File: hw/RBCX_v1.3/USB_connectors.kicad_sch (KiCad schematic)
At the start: 24 parts, among them J49 Conn_01x04, J50 Conn_01x04, U21 USB_C, U22 AP33772

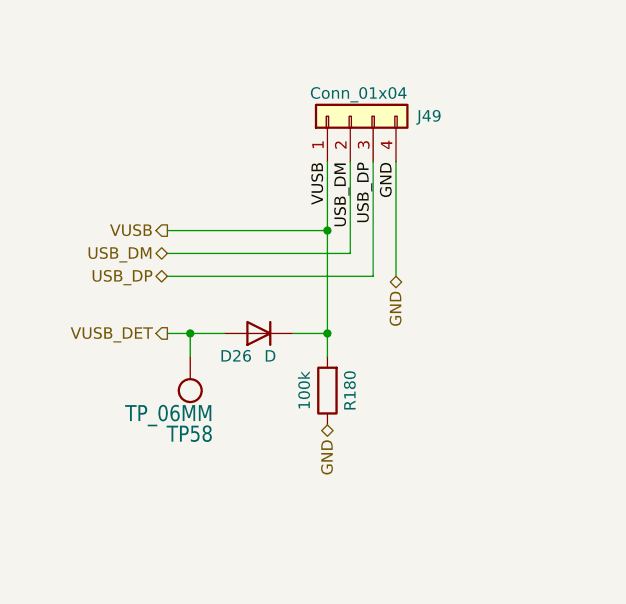
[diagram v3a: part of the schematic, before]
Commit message: USB-DET level shifter
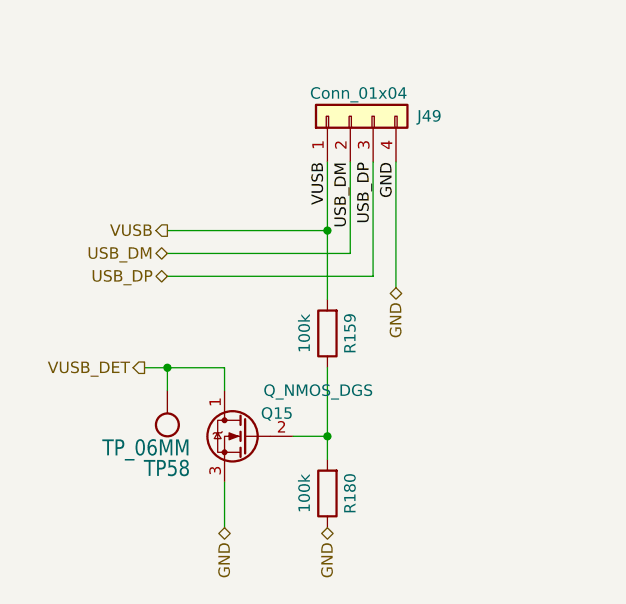
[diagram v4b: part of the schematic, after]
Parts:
- removed D26: D, Diode_SMD:D_SOD-523, symbol Device:D
- added Q15: Q_NMOS_DGS, Package_TO_SOT_SMD:SOT-723, symbol Device:Q_NMOS_DGS
- added R159: 100k, Capacitor_SMD:C_0201_0603Metric, symbol Device:R
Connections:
- net GND: now also Q15.3 (S)
- net VUSB: now also R159.2; no longer R180.2
- net VUSB_DET: now also Q15.1 (D)
- new net: Q15.2 (G), R159.1, R180.2
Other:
- moved on the sheet: R180, TP58
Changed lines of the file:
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@@
   (junction (at 220.98 54.61) (diameter 0) (color 0 0 0 0)
   )
-  (junction (at 86.36 140.97) (diameter 0) (color 0 0 0 0)
+  (junction (at 83.82 144.78) (diameter 0) (color 0 0 0 0)
   )
   (junction (at 153.67 44.45) (diameter 0) (color 0 0 0 0)
@@
   (junction (at 173.99 62.23) (diameter 0) (color 0 0 0 0)
   )
-  (junction (at 101.6 140.97) (diameter 0) (color 0 0 0 0)
+  (junction (at 101.6 152.4) (diameter 0) (color 0 0 0 0)
   )
   (junction (at 82.55 64.77) (diameter 0) (color 0 0 0 0)
@@
     (stroke (width 0) (type default) (color 0 0 0 0))
   )
-  (wire (pts (xy 86.36 140.97) (xy 90.17 140.97))
-    (stroke (width 0) (type default) (color 0 0 0 0))
-  )
   (wire (pts (xy 153.67 44.45) (xy 163.83 44.45))
     (stroke (width 0) (type default) (color 0 0 0 0))
@@
     (stroke (width 0) (type default) (color 0 0 0 0))
   )
+  (wire (pts (xy 83.82 144.78) (xy 90.17 144.78))
+    (stroke (width 0) (type default) (color 0 0 0 0))
+  )
   (wire (pts (xy 132.08 78.74) (xy 132.08 76.2))
     (stroke (width 0) (type default) (color 0 0 0 0))
@@
     (stroke (width 0) (type default) (color 0 0 0 0))
   )
-  (wire (pts (xy 101.6 140.97) (xy 101.6 143.51))
+  (wire (pts (xy 101.6 152.4) (xy 101.6 154.94))
     (stroke (width 0) (type default) (color 0 0 0 0))
   )
@@
     (stroke (width 0) (type default) (color 0 0 0 0))
   )
+  (wire (pts (xy 101.6 144.78) (xy 101.6 152.4))
+    (stroke (width 0) (type default) (color 0 0 0 0))
+  )
   (wire (pts (xy 189.23 67.31) (xy 173.99 67.31))
     (stroke (width 0) (type default) (color 0 0 0 0))
@@
     (stroke (width 0) (type default) (color 0 0 0 0))
   )
-  (wire (pts (xy 109.22 121.92) (xy 109.22 134.62))
+  (wire (pts (xy 109.22 121.92) (xy 109.22 135.89))
     (stroke (width 0) (type default) (color 0 0 0 0))
   )
@@
     (stroke (width 0) (type default) (color 0 0 0 0))
   )
-  (wire (pts (xy 83.82 140.97) (xy 86.36 140.97))
+  (wire (pts (xy 90.17 144.78) (xy 90.17 147.32))
+    (stroke (width 0) (type default) (color 0 0 0 0))
+  )
+  (wire (pts (xy 81.28 144.78) (xy 83.82 144.78))
     (stroke (width 0) (type default) (color 0 0 0 0))
   )
@@
     (stroke (width 0) (type default) (color 0 0 0 0))
   )
-  (wire (pts (xy 97.79 140.97) (xy 101.6 140.97))
+  (wire (pts (xy 97.79 152.4) (xy 101.6 152.4))
     (stroke (width 0) (type default) (color 0 0 0 0))
   )
@@
     (stroke (width 0) (type default) (color 0 0 0 0))
   )
-  (wire (pts (xy 101.6 140.97) (xy 101.6 129.54))
+  (wire (pts (xy 101.6 129.54) (xy 101.6 137.16))
     (stroke (width 0) (type default) (color 0 0 0 0))
   )
@@
     (stroke (width 0) (type default) (color 0 0 0 0))
   )
-  (wire (pts (xy 86.36 143.51) (xy 86.36 140.97))
+  (wire (pts (xy 83.82 147.32) (xy 83.82 144.78))
     (stroke (width 0) (type default) (color 0 0 0 0))
   )
@@
   )
   (wire (pts (xy 76.2 54.61) (xy 76.2 76.2))
+    (stroke (width 0) (type default) (color 0 0 0 0))
+  )
+  (wire (pts (xy 90.17 162.56) (xy 90.17 157.48))
     (stroke (width 0) (type default) (color 0 0 0 0))
   )
@@
     (effects (font (size 1.27 1.27)) (justify right))
   )
+  (hierarchical_label "GND" (shape bidirectional) (at 90.17 162.56 270)
+    (effects (font (size 1.27 1.27)) (justify right))
+  )
   (hierarchical_label "GND" (shape input) (at 248.92 102.87 270)
     (effects (font (size 1.27 1.27)) (justify right))
@@
     (effects (font (size 1.27 1.27)) (justify right))
   )
-  (hierarchical_label "VUSB_DET" (shape output) (at 83.82 140.97 180)
+  (hierarchical_label "VUSB_DET" (shape output) (at 81.28 144.78 180)
     (effects (font (size 1.27 1.27)) (justify right))
   )
@@
     (effects (font (size 1.27 1.27)) (justify right))
   )
-  (hierarchical_label "GND" (shape bidirectional) (at 109.22 134.62 270)
+  (hierarchical_label "GND" (shape bidirectional) (at 109.22 135.89 270)
     (effects (font (size 1.27 1.27)) (justify right))
   )
@@
     (effects (font (size 1.27 1.27)) (justify right))
   )
-  (hierarchical_label "GND" (shape bidirectional) (at 101.6 151.13 270)
+  (hierarchical_label "GND" (shape bidirectional) (at 101.6 162.56 270)
     (effects (font (size 1.27 1.27)) (justify right))
   )
@@
     (pin "2")
   )
-  (symbol (lib_id "Device:R") (at 101.6 147.32 180) (unit 1)
-    (in_bom yes) (on_board yes)
-    (property "Reference" "R180" (id 0) (at 104.14 147.32 90))
-    (property "Value" "100k" (id 1) (at 99.06 147.32 90))
-    (property "Footprint" "Capacitor_SMD:C_0201_0603Metric" (id 2) (at 103.378 147.32 90)
-      (effects (font (size 1.27 1.27)) hide)
-    )
-    (property "Datasheet" "~" (id 3) (at 101.6 147.32 0)
-      (effects (font (size 1.27 1.27)) hide)
-    )
-    (property "LCSC" "C270364" (id 4) (at 101.6 147.32 0)
-      (effects (font (size 1.27 1.27)) hide)
-    )
-    (property "Basic/Extended" "E" (id 5) (at 101.6 147.32 0)
+  (symbol (lib_id "Device:R") (at 101.6 158.75 180) (unit 1)
+    (in_bom yes) (on_board yes)
+    (property "Reference" "R180" (id 0) (at 104.14 158.75 90))
+    (property "Value" "100k" (id 1) (at 99.06 158.75 90))
+    (property "Footprint" "Capacitor_SMD:C_0201_0603Metric" (id 2) (at 103.378 158.75 90)
+      (effects (font (size 1.27 1.27)) hide)
+    )
+    (property "Datasheet" "~" (id 3) (at 101.6 158.75 0)
+      (effects (font (size 1.27 1.27)) hide)
+    )
+    (property "LCSC" "C270364" (id 4) (at 101.6 158.75 0)
+      (effects (font (size 1.27 1.27)) hide)
+    )
+    (property "Basic/Extended" "E" (id 5) (at 101.6 158.75 0)
       (effects (font (size 1.27 1.27)) hide)
     )
@@
     (pin "3")
     (pin "4")
+  )
+  (symbol (lib_id "Device:R") (at 101.6 140.97 180) (unit 1)
+    (in_bom yes) (on_board yes)
+    (property "Reference" "R159" (id 0) (at 104.14 140.97 90))
+    (property "Value" "100k" (id 1) (at 99.06 140.97 90))
+    (property "Footprint" "Capacitor_SMD:C_0201_0603Metric" (id 2) (at 103.378 140.97 90)
+      (effects (font (size 1.27 1.27)) hide)
+    )
+    (property "Datasheet" "~" (id 3) (at 101.6 140.97 0)
+      (effects (font (size 1.27 1.27)) hide)
+    )
+    (property "LCSC" "C270364" (id 4) (at 101.6 140.97 0)
+      (effects (font (size 1.27 1.27)) hide)
+    )
+    (property "Basic/Extended" "E" (id 5) (at 101.6 140.97 0)
+      (effects (font (size 1.27 1.27)) hide)
+    )
+    (pin "1")
+    (pin "2")
   )
   (symbol (lib_id "Device:R") (at 248.92 99.06 180) (unit 1)
@@
     (pin "4")
   )
-  (symbol (lib_id "RBCX-eagle-import:TP_06MM") (at 86.36 143.51 180) (unit 1)
-    (in_bom yes) (on_board yes)
-    (property "Reference" "TP58" (id 0) (at 88.9 151.13 0)
+  (symbol (lib_id "RBCX-eagle-import:TP_06MM") (at 83.82 147.32 180) (unit 1)
+    (in_bom yes) (on_board yes)
+    (property "Reference" "TP58" (id 0) (at 86.36 154.94 0)
       (effects (font (size 1.778 1.5113)) (justify left bottom))
     )
-    (property "Value" "TP_06MM" (id 1) (at 88.9 148.844 0)
+    (property "Value" "TP_06MM" (id 1) (at 86.36 152.654 0)
       (effects (font (size 1.778 1.5113)) (justify left bottom))
     )
-    (property "Footprint" "RBCX:TP_06MM" (id 2) (at 86.36 143.51 0)
-      (effects (font (size 1.27 1.27)) hide)
-    )
-    (property "Datasheet" "" (id 3) (at 86.36 143.51 0)
-      (effects (font (size 1.27 1.27)) hide)
-    )
-    (property "JLCPCB_IGNORE" "1" (id 4) (at 86.36 143.51 0)
+    (property "Footprint" "RBCX:TP_06MM" (id 2) (at 83.82 147.32 0)
+      (effects (font (size 1.27 1.27)) hide)
+    )
+    (property "Datasheet" "" (id 3) (at 83.82 147.32 0)
+      (effects (font (size 1.27 1.27)) hide)
+    )
+    (property "JLCPCB_IGNORE" "1" (id 4) (at 83.82 147.32 0)
       (effects (font (size 1.27 1.27)) hide)
     )
     (pin "P$1")
-  )
-  (symbol (lib_id "Device:D") (at 93.98 140.97 180) (unit 1)
-    (in_bom yes) (on_board yes)
-    (property "Reference" "D26" (id 0) (at 91.44 143.51 0))
-    (property "Value" "D" (id 1) (at 95.25 143.51 0))
-    (property "Footprint" "Diode_SMD:D_SOD-523" (id 2) (at 93.98 140.97 0)
-      (effects (font (size 1.27 1.27)) hide)
-    )
-    (property "Datasheet" "https://datasheet.lcsc.com/lcsc/1809200051_Jiangsu-Changjing-Electronics-Technology-Co---Ltd--1N4148WT-T4_C68948.pdf" (id 3) (at 93.98 140.97 0)
-      (effects (font (size 1.27 1.27)) hide)
-    )
-    (property "LCSC" "C68948" (id 4) (at 93.98 140.97 0)
-      (effects (font (size 1.27 1.27)) hide)
-    )
-    (property "Basic/Extended" "E" (id 5) (at 93.98 140.97 0)
-      (effects (font (size 1.27 1.27)) hide)
-    )
-    (pin "1")
-    (pin "2")
   )
   (symbol (lib_id "Device:C") (at 142.24 50.8 0) (unit 1)
@@
     (pin "B9")
   )
+  (symbol (lib_id "Device:Q_NMOS_DGS") (at 92.71 152.4 0) (mirror y) (unit 1)
+    (in_bom yes) (on_board yes)
+    (property "Reference" "Q15" (id 0) (at 97.79 149.86 0)
+      (effects (font (size 1.27 1.27)) (justify left))
+    )
+    (property "Value" "Q_NMOS_DGS" (id 1) (at 106.68 147.32 0)
+      (effects (font (size 1.27 1.27)) (justify left))
+    )
+    (property "Footprint" "Package_TO_SOT_SMD:SOT-723" (id 2) (at 87.63 149.86 0)
+      (effects (font (size 1.27 1.27)) hide)
+    )
+    (property "Datasheet" "https://datasheet.lcsc.com/lcsc/2004141706_Jiangsu-Changjing-Electronics-Technology-Co---Ltd--2SK3541_C504051.pdf" (id 3) (at 92.71 152.4 0)
+      (effects (font (size 1.27 1.27)) hide)
+    )
+    (property "LCSC" "C504051" (id 4) (at 92.71 152.4 0)
+      (effects (font (size 1.27 1.27)) hide)
+    )
+    (property "Basic/Extended" "E" (id 5) (at 92.71 152.4 0)
+      (effects (font (size 1.27 1.27)) hide)
+    )
+    (property "JLCPCB_CORRECTION" "0;0;180" (id 6) (at 92.71 152.4 0)
+      (effects (font (size 1.27 1.27)) hide)
+    )
+    (pin "1")
+    (pin "2")
+    (pin "3")
+  )
   (symbol (lib_id "Device:LED") (at 240.03 91.44 90) (unit 1)

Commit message: ESD and I-Servo hacker
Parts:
- added D26: PTVSHC3N24, Robotarna_KiCad_Library:DFN3-2x2, symbol Robotarna_KiCad_Library:PTVSHC3N24
- added U23: TPD4E02B04DQA, Package_SON:USON-10_2.5x1.0mm_P0.5mm, symbol Power_Protection:TPD4E02B04DQA
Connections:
- net GND: now also D26.1 (A), D26.2 (A), U23.3 (G), U23.8 (G)
- net USB_CC1: now also U23.5 (IO4)
- net USB_CC2: now also U23.4 (IO3)
- net USB_DM: now also U23.2 (IO2)
- net USB_DP: now also U23.1 (IO1)
- net VUSB: now also D26.3 (K)
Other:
- moved on the sheet: C77, C78, C79, C80, C81, C82, D41, D42, D43, D44, J50, R172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
